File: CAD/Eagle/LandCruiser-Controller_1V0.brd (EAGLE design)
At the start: 99 x 67.7 mm, 37 parts, among them U101 MEGA8-P, U221 SN75240, U301 MIC2981/2982, U511 LM7805, X201 WEIDMUELLER 1234600000, X321 WEIDMUELLER 1234600000, X401 I2C

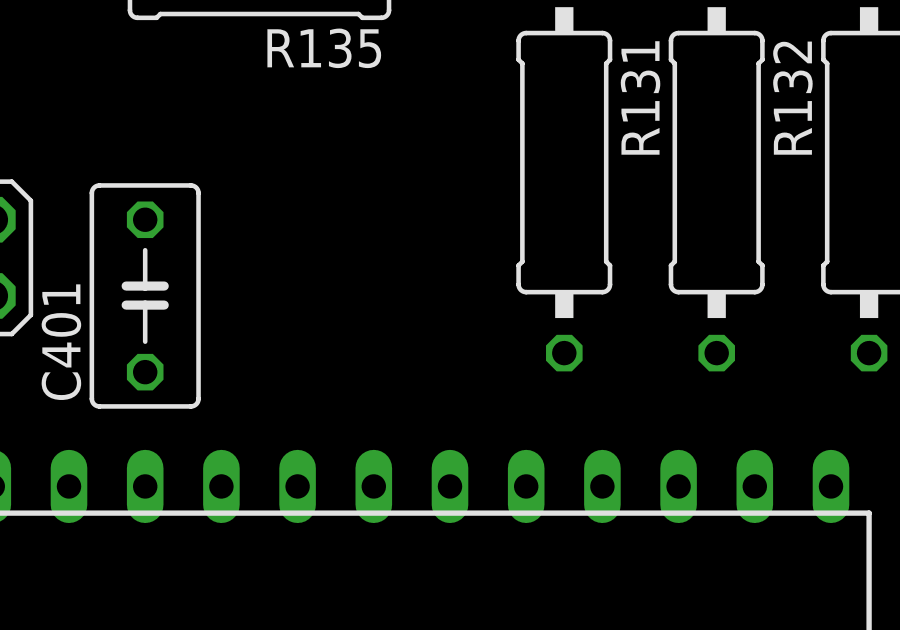
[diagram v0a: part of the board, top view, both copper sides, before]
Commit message: HW_V1.0 - MPU - AVCC with 10uH for better ADC results
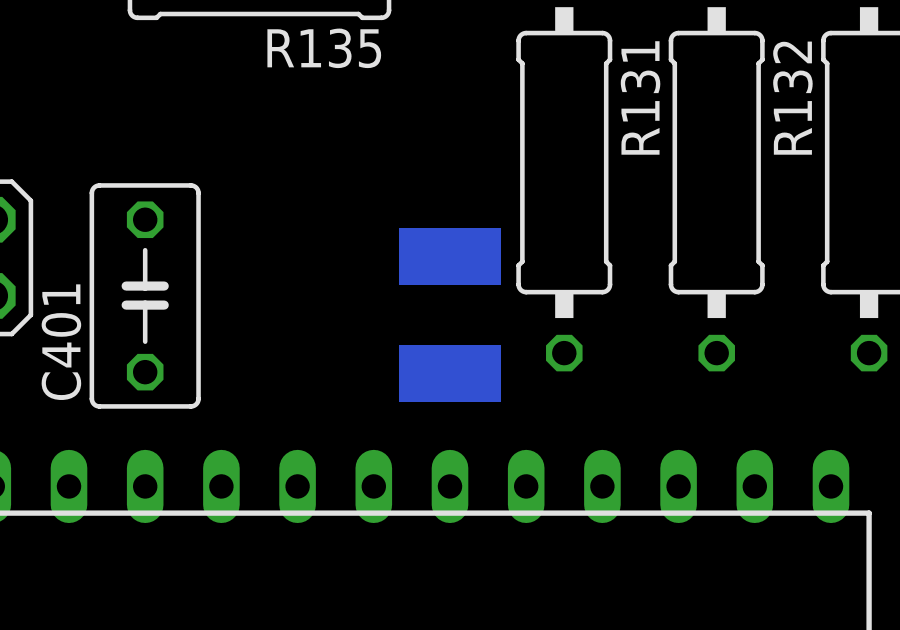
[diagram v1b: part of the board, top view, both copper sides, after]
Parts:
- added L101: 10uH, rcl:L1812
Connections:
- net AREF renamed MP_AREF
- new net MP_AVCC: L101.1, U101.20
- net +5V: now also L101.2; no longer U101.20
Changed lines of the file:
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@@
 <element name="U221" library="df4iah_esd" package="TSSOP-8" value="SN75240" x="27.94" y="5.08"/>
 <element name="U301" library="df4iah_dataconvertion" package="DIL18" value="MIC2981/2982" x="86.36" y="25.4" rot="R90"/>
+<element name="L101" library="rcl" package="L1812" value="10uH" x="62.23" y="43.18" rot="MR90"/>
 </elements>
 <signals>
@@
 <contactref element="R492" pad="2"/>
 <contactref element="R101" pad="1"/>
-<contactref element="U101" pad="20"/>
 <contactref element="U101" pad="7"/>
 <contactref element="R123" pad="2"/>
@@
 <contactref element="C521" pad="+"/>
 <contactref element="C101" pad="1"/>
+<contactref element="L101" pad="2"/>
 <wire x1="27.94" y1="63.5" x2="36.83" y2="63.5" width="0" layer="19" extent="1-1"/>
 <wire x1="36.83" y1="43.18" x2="36.83" y2="63.5" width="0" layer="19" extent="1-1"/>
@@
 <wire x1="44.45" y1="43.815" x2="36.83" y2="43.18" width="0" layer="19" extent="1-1"/>
 <wire x1="52.07" y1="41.275" x2="44.45" y2="43.815" width="0" layer="19" extent="1-1"/>
-<wire x1="62.23" y1="37.465" x2="52.07" y2="41.275" width="0" layer="19" extent="1-1"/>
-<wire x1="57.15" y1="29.845" x2="62.23" y2="37.465" width="0" layer="19" extent="1-1"/>
+<wire x1="57.15" y1="29.845" x2="52.07" y2="41.275" width="0" layer="19" extent="1-1"/>
 <wire x1="55.88" y1="24.765" x2="57.15" y2="29.845" width="0" layer="19" extent="1-1"/>
 <wire x1="49.53" y1="12.7" x2="55.88" y2="24.765" width="0" layer="19" extent="1-1"/>
@@
 <wire x1="67.31" y1="12.7" x2="55.88" y2="24.765" width="0" layer="19" extent="1-1"/>
 <wire x1="72.39" y1="12.7" x2="67.31" y2="12.7" width="0" layer="19" extent="1-1"/>
+<wire x1="62.23" y1="45.13" x2="31.75" y2="21.59" width="0" layer="19" extent="1-1"/>
 </signal>
 <signal name="SCL">
@@
 <wire x1="34.29" y1="26.67" x2="41.91" y2="25.4" width="0" layer="19" extent="1-1"/>
 </signal>
-<signal name="AREF">
+<signal name="MP_AREF">
 <contactref element="C102" pad="2"/>
 <contactref element="U101" pad="21"/>
@@
 <contactref element="U301" pad="14"/>
 </signal>
+<signal name="MP_AVCC">
+<contactref element="U101" pad="20"/>
+<contactref element="L101" pad="1"/>
+<wire x1="62.23" y1="41.23" x2="62.23" y2="37.465" width="0" layer="19" extent="1-1"/>
+</signal>
 </signals>

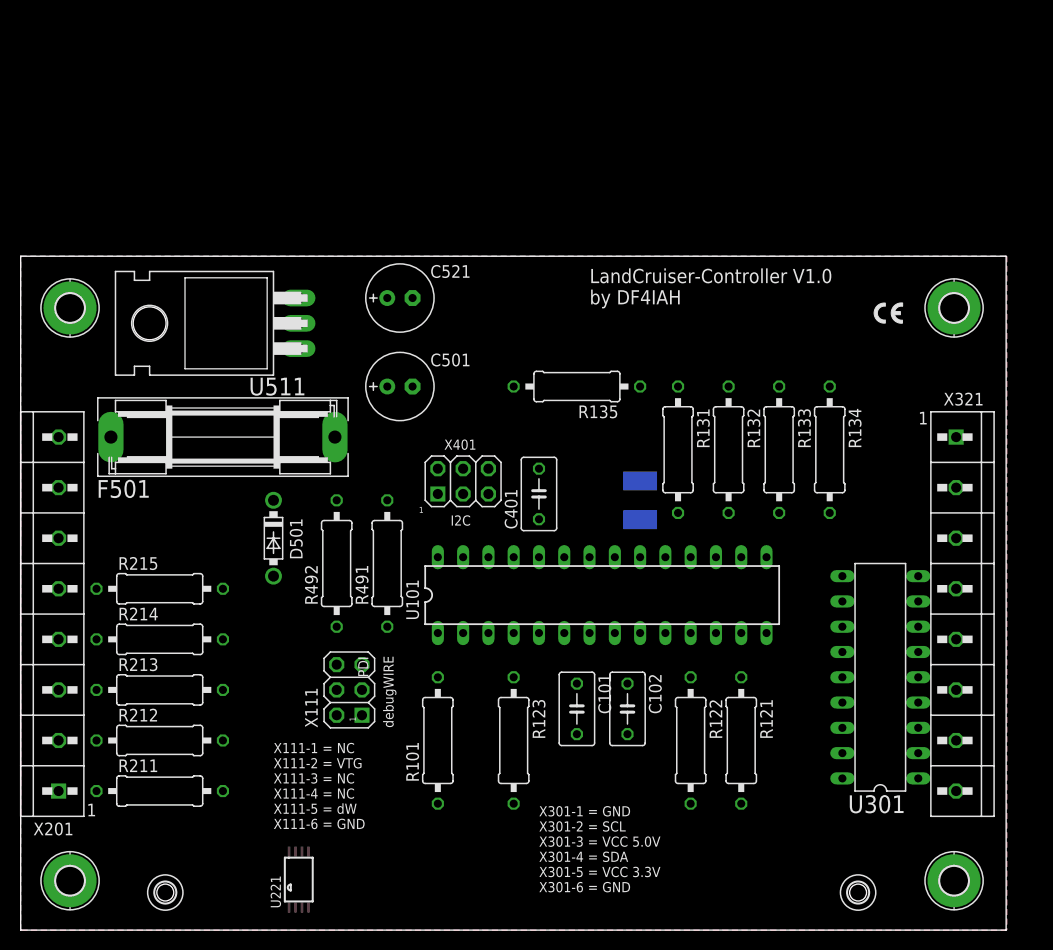
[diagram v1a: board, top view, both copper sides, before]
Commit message: HW_V1.0 - OUTPUT - relay units added
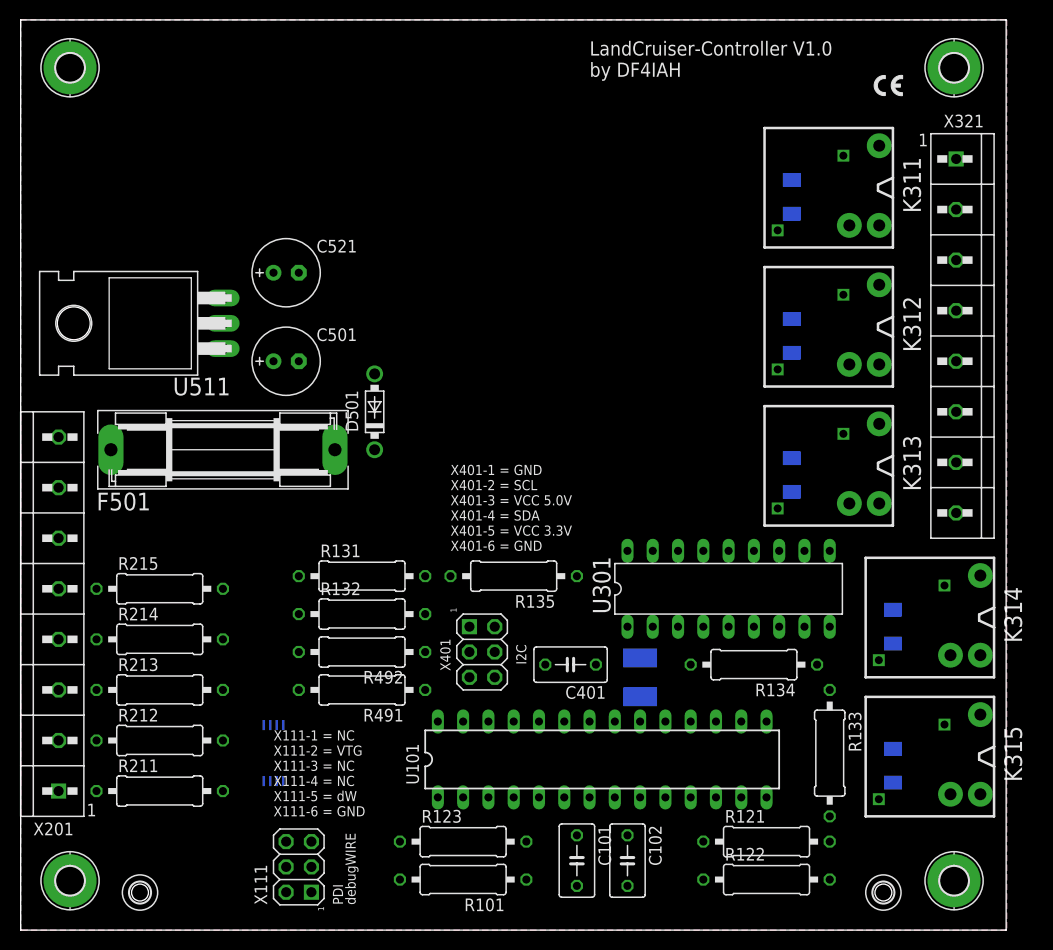
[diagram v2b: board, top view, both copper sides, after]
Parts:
- added D311, D312, D313, D314, D315: CRS08, df4iah_diode:SOD80C
- added K311, K312, K313, K314, K315: V23086C1001A403, df4iah_relay:V23086-CO
- F501: device fuse:SH22,5 -> df4iah_fuse:SH22,5
- moved R132 40.4 mm to (34.3, 31.8), turned to 0 degrees
- moved R131 34.2 mm to (34.3, 35.6), turned to 0 degrees
- moved R133 30.9 mm to (81.3, 17.8)
- moved X321 27.9 mm to (94.0, 59.7)
- moved H601 24.1 mm to (4.96, 86.6)
- moved H602 24.1 mm to (93.8, 86.6)
- moved R134 22.9 mm to (73.7, 26.7), turned to 180 degrees
- moved R135 20.1 mm to (49.5, 35.6)
- moved X111 18.5 mm to (27.9, 6.35)
- moved L101 17.8 mm to (62.2, 25.4)
- moved U301 17.6 mm to (71.1, 34.3), turned to 0 degrees
- moved C401 17.4 mm to (55.2, 26.7), turned to 180 degrees
- moved X401 17.3 mm to (46.4, 27.9), turned to 270 degrees
- moved U101 16.5 mm to (58.4, 17.1)
- moved D501 16.3 mm to (35.6, 52.1), turned to 90 degrees
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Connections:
- net +12V: now also D311.C, D312.C, D313.C, D314.C, D315.C, K311.1, K311.5, K312.1, K312.5, K313.1, K313.5, K314.1, K314.5, K315.1, K315.5
- net DRV_KL: now also D311.A, K311.2
- net DRV_M1: now also D314.A, K314.2
- net DRV_M2: now also D315.A, K315.2
- net DRV_PV_G: now also D312.A, K312.2
- net DRV_PV_O: now also D313.A, K313.2
- net GND: now also K314.3, K315.3, X201.6, X321.6, X321.7
- net KL: now also K311.4
- net M1: now also K314.4
- net M2: now also K315.4
- net PV_G: now also K312.4
- net PV_O: now also K313.4
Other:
- board size 99 x 67.7 mm -> 99 x 91.4 mm
- board text added: "X401-1 = GND X401-2 = SCL X401-3 = VCC 5.0V X401-4 = SDA X401-5 = VCC 3.3V X401-6 = GND"
- board text removed: "X301-1 = GND X301-2 = SCL X301-3 = VCC 5.0V X301-4 = SDA X301-5 = VCC 3.3V X301-6 = GND"

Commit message: HW_V1.0 - V24 level shifter connected, Tacho input signal added
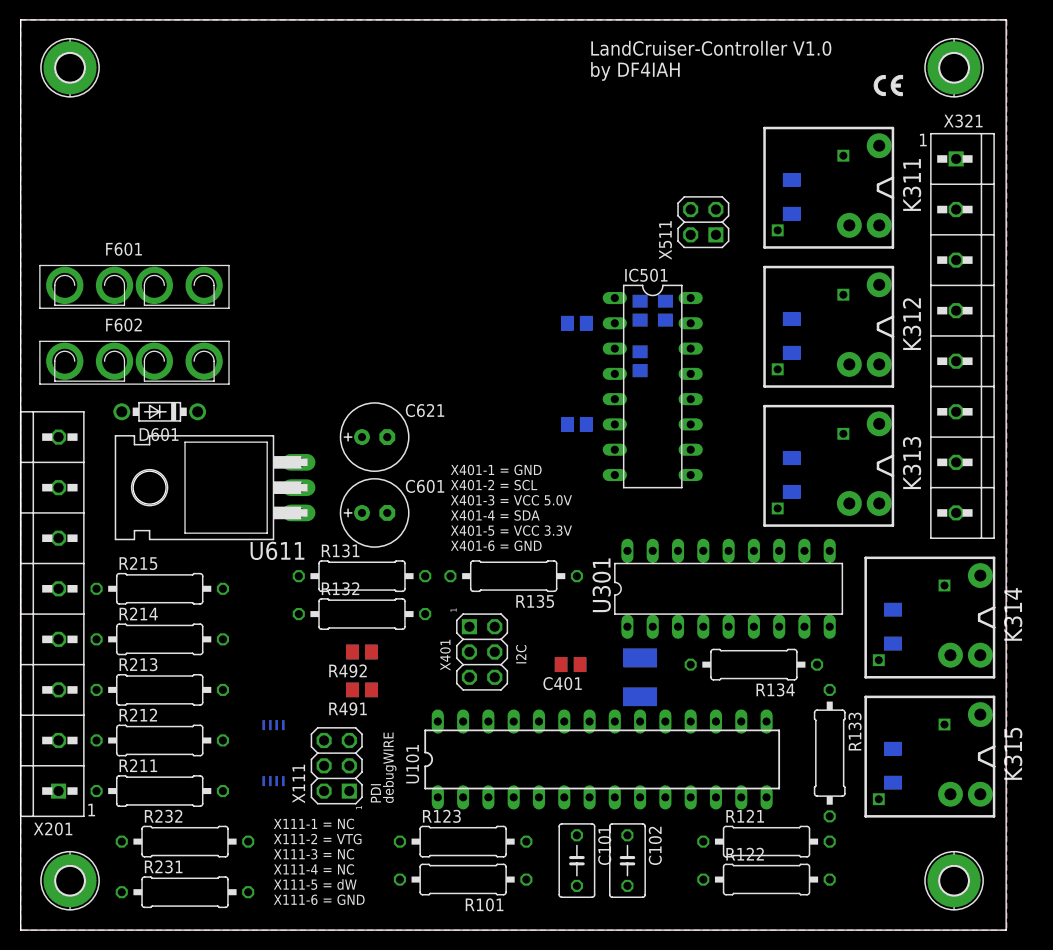
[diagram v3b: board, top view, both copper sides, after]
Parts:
- removed C521: 22uF, rcl:E2,5-7
- removed D501: 1N5817-B, df4iah_diode:DO41-7.6
- removed F501: 500 mA (S), df4iah_fuse:SH22,5
- removed H611, H612: MOUNT-HOLE1.7, df4iah_holes:1,7
- removed U511: LM7805, df4iah_powersupply:TO220H
- added C502, C503, C504, C511: 1uF, rcl:C0805
- added C601, C621: 22uF, rcl:E2,5-7
- added D601: 1N5817-B, df4iah_diode:DO41-7.6
- added F601: 15 A (S), df4iah_fuse:MCCQ-121
- added F602: 500 mA (S), df4iah_fuse:MCCQ-121
- added IC501: MAX232, df4iah_dataconvertion:DIL16
- added R231: 10kR, rcl:0309/12
- added R232: 22kR, rcl:0309/12
- added U611: LM7805, df4iah_powersupply:TO220H
- added X511: (no value), df4iah_connector:2X02
- C401: device rcl:C050-035X075 -> rcl:C0805
- C501: value 22uF -> 1uF; device rcl:E2,5-7 -> rcl:C0805
- R491, R492: device rcl:0309/12 -> rcl:R0805
- moved C501 35.9 mm to (62.2, 62.2), flipped to the bottom, turned to 270 degrees
- moved X111 10.9 mm to (31.8, 16.5)
- renumbered H601 to H701, H602 to H702, H603 to H703, H604 to H704
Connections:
- new net MP_TACHO: R231.2, R232.1, U101.25
- new net MX_C1N: C501.2, IC501.3
- new net MX_C1P: C501.1, IC501.1
- new net MX_C2M: C502.2, IC501.5
- new net MX_C2P: C502.1, IC501.4
- new net MX_VM: C504.1, IC501.6
- new net MX_VP: C503.1, IC501.2
- new net N$1: C601.+, D601.C, F602.P$3, F602.P$4, U611.1
- new net RXD: IC501.13, X511.2
- new net TACHO: R232.2, X201.1
- new net TXD: IC501.14, X511.1
- net +12V: now also F601.P$3, F601.P$4; no longer C501.+, D501.C, F501.2, U511.1
- net +5V: now also C511.1, C621.+, IC501.16, U611.3; no longer C521.+, U511.3
- net +UB: now also F601.P$1, F601.P$2, F602.P$1, F602.P$2; no longer F501.1
- net ECU_FB: now also X201.2; no longer X201.1
- net GND: now also C503.2, C504.2, C511.2, C601.-, C621.-, D601.A, IC501.10, IC501.15, IC501.8, R231.1, U611.2; no longer C501.-, C521.-, D501.A, U511.2, X201.6
- net MP_RXD: now also IC501.12
- net MP_TXD: now also IC501.11
- net SA_G: now also X201.5; no longer X201.4
- net SA_O: now also X201.6; no longer X201.5
- net SK_G: now also X201.3; no longer X201.2
- net SK_O: now also X201.4; no longer X201.3

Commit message: HW_V1.0 - changed most devices to SMD variants
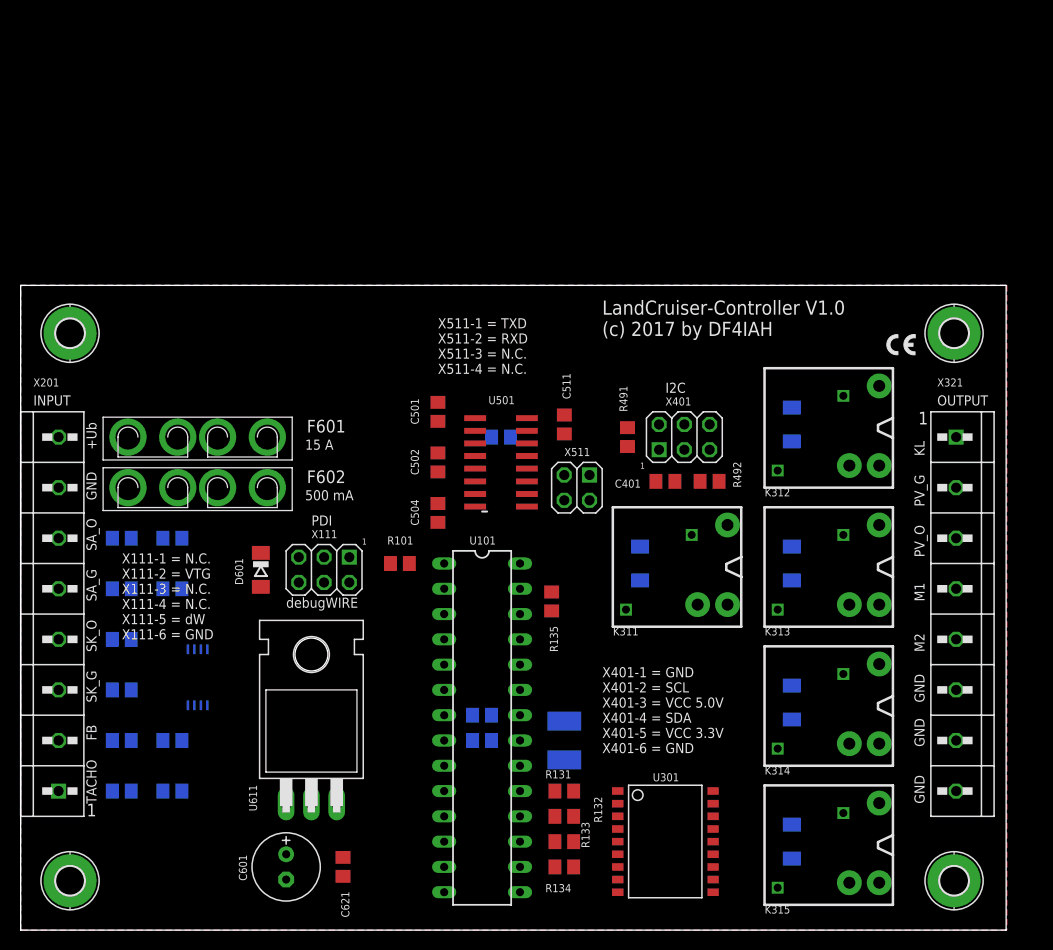
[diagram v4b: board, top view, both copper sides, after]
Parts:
- removed IC501: MAX232, df4iah_dataconvertion:DIL16
- added U501: MAX232_SOIC16, df4iah_dataconvertion:SOIC16N
- C101, C102: device rcl:C050-035X075 -> rcl:C0805
- C621: device rcl:E2,5-7 -> rcl:C0805
- D601: value 1N5817-B -> CRS08; device df4iah_diode:DO41-7.6 -> df4iah_diode:SOD80C
- R101, R121, R122, R123, R131, R132, R133, R134, R135, R211, R212, R213, R214, R215, R231, R232: device rcl:0309/12 -> rcl:R0805
- U301: value MIC2981/2982 -> MIC2981/2982SO18W; device df4iah_dataconvertion:DIL18 -> df4iah_dataconvertion:SO-18W
- moved R121 67.0 mm to (15.2, 39.4), flipped to the bottom, turned to 180 degrees
- moved R122 66.5 mm to (15.2, 34.3), flipped to the bottom, turned to 180 degrees
- moved C621 43.3 mm to (32.4, 6.35), turned to 270 degrees
- moved K311 41.0 mm to (72.4, 30.5)
- moved D311 39.9 mm to (62.2, 36.8)
- moved R492 38.9 mm to (69.2, 45.1)
- moved R491 36.8 mm to (61.0, 49.5), turned to 270 degrees
- moved C601 36.7 mm to (26.7, 6.35), turned to 270 degrees
- moved R101 32.4 mm to (38.1, 36.8), turned to 0 degrees
- moved R123 30.9 mm to (15.2, 19.1), flipped to the bottom, turned to 180 degrees
- moved R131 29.6 mm to (54.6, 14.0), turned to 180 degrees
- moved X401 29.6 mm to (66.7, 49.5), turned to 0 degrees
- moved X511 29.5 mm to (55.9, 44.5), turned to 180 degrees
- moved R132 28.7 mm to (54.6, 11.4), turned to 180 degrees
- moved R133 28.1 mm to (54.6, 8.89), turned to 180 degrees
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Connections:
- net N$1 renamed REGIN
- net +5V: now also C621.1, U501.16; no longer C621.+, IC501.16
- net GND: now also C621.2, U501.10, U501.15, U501.8; no longer C621.-, IC501.10, IC501.15, IC501.8
- net MP_RXD: now also U501.12; no longer IC501.12
- net MP_TXD: now also U501.11; no longer IC501.11
- net MX_C1N: now also U501.3; no longer IC501.3
- net MX_C1P: now also U501.1; no longer IC501.1
- net MX_C2M: now also U501.5; no longer IC501.5
- net MX_C2P: now also U501.4; no longer IC501.4
- net MX_VM: now also U501.6; no longer IC501.6
- net MX_VP: now also U501.2; no longer IC501.2
- net RXD: now also U501.13; no longer IC501.13
- net TXD: now also U501.14; no longer IC501.14
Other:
- board size 99 x 91.4 mm -> 99 x 64.8 mm
- board text added: "+Ub"
- board text added: "15 A"
- board text added: "500 mA"
- board text added: "FB"
- board text added: "GND"
- board text added: "INPUT"
- board text added: "KL"
- board text added: "LandCruiser-Controller V1.0 (c) 2017 by DF4IAH"
- board text added: "M1"
- board text added: "M2"
- board text added: "OUTPUT"
- board text added: "PV_G"
- board text added: "PV_O"
- board text added: "SA_G"
- board text added: "SA_O"
- board text added: "SK_G"
- board text added: "SK_O"
- board text added: "TACHO"
- board text added: "X111-1 = N.C. X111-2 = VTG X111-3 = N.C. X111-4 = N.C. X111-5 = dW X111-6 = GND"
- board text added: "X511-1 = TXD X511-2 = RXD X511-3 = N.C. X511-4 = N.C."
- board text removed: "LandCruiser-Controller V1.0 by DF4IAH"
- board text removed: "X111-1 = NC X111-2 = VTG X111-3 = NC X111-4 = NC X111-5 = dW X111-6 = GND"

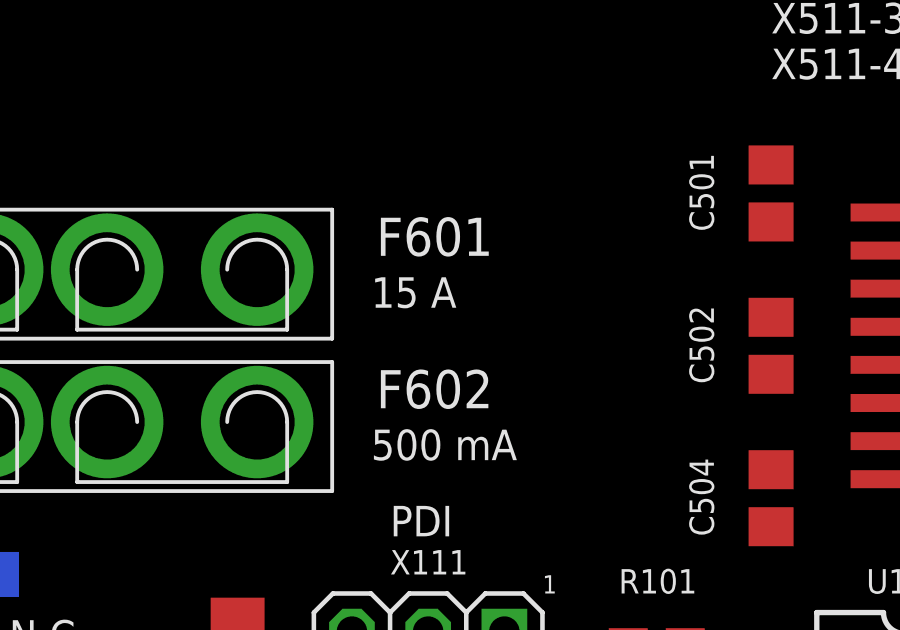
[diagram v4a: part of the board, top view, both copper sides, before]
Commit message: HW_V1.0 - df4iah_fuse.lbr - trying to fix the restring issue
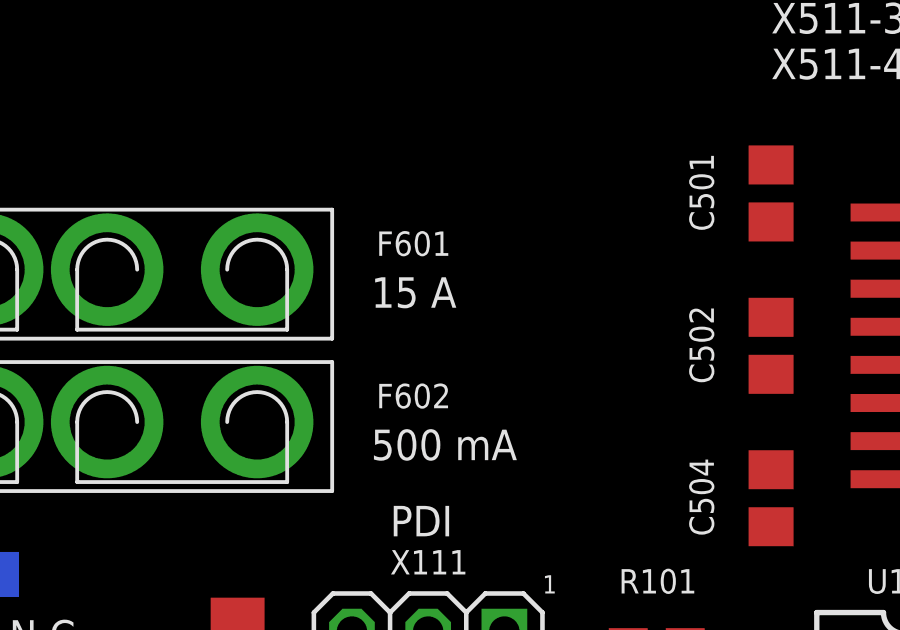
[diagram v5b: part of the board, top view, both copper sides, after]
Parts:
- F601: value 15 A (S) -> 15 A
- F602: value 500 mA (S) -> 500 mA
